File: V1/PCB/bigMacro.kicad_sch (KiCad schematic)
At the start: 24 parts, among them SW1 SW_Push, U1 ATmega32U4-A, Y1 16MHz

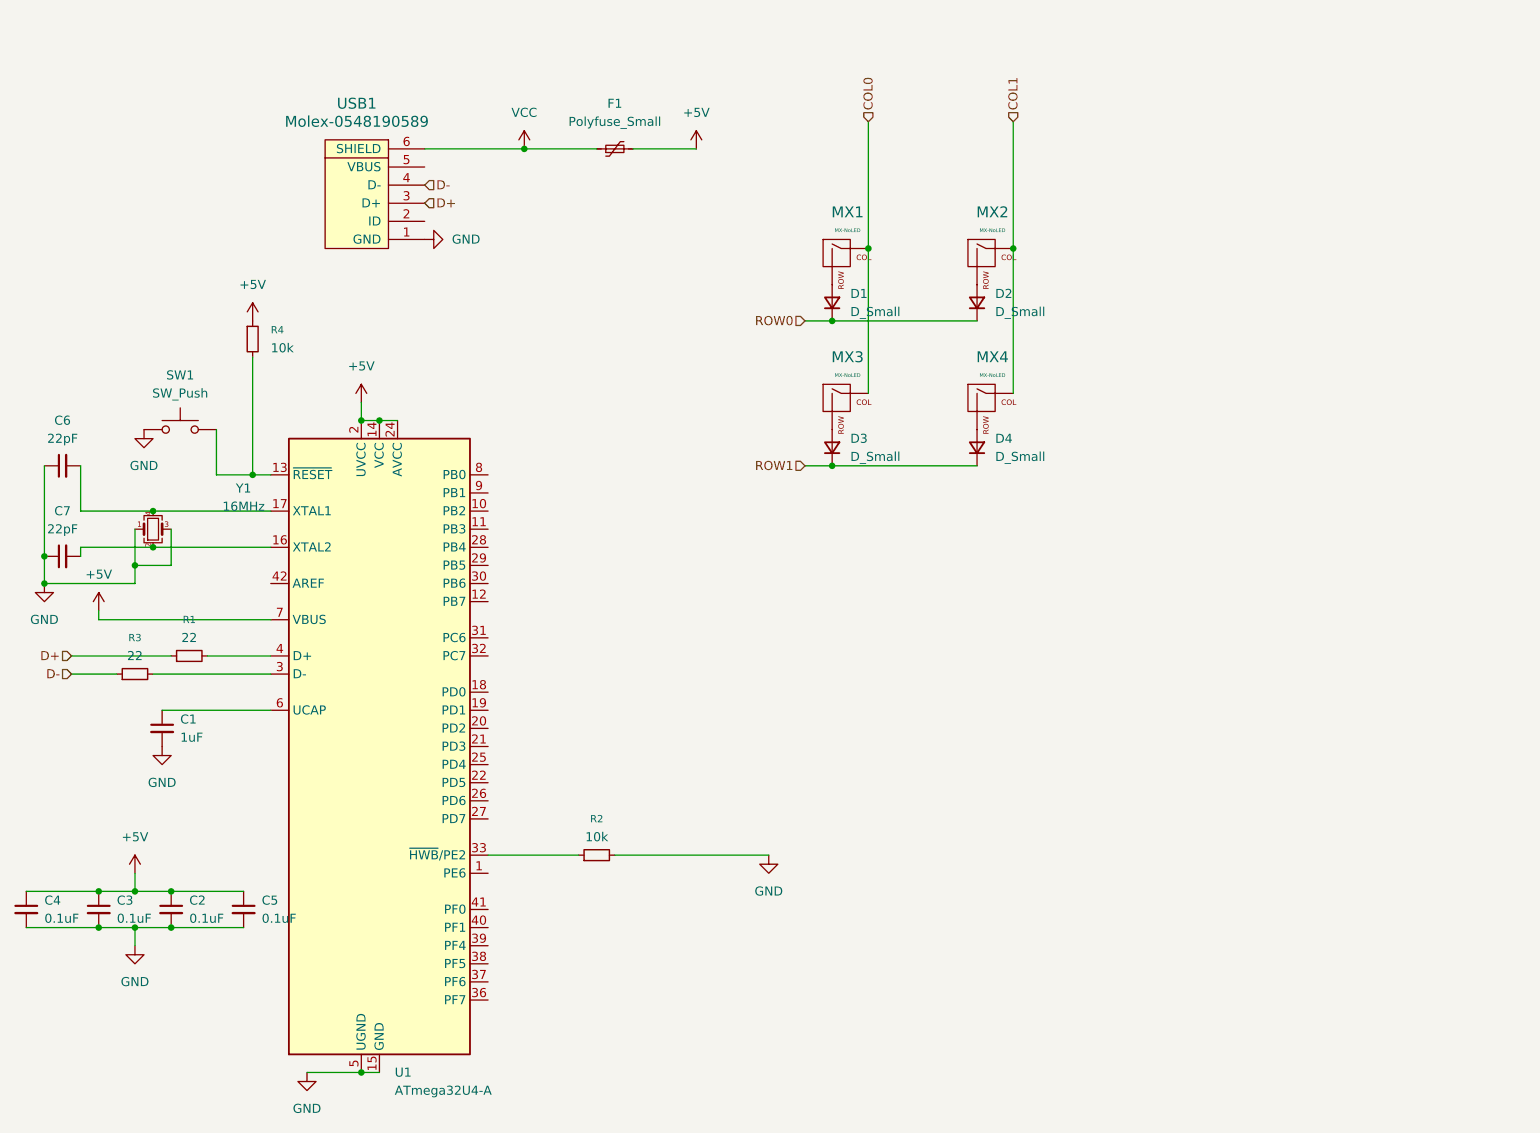
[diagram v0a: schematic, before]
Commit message: Update PCB Layout based on requirements
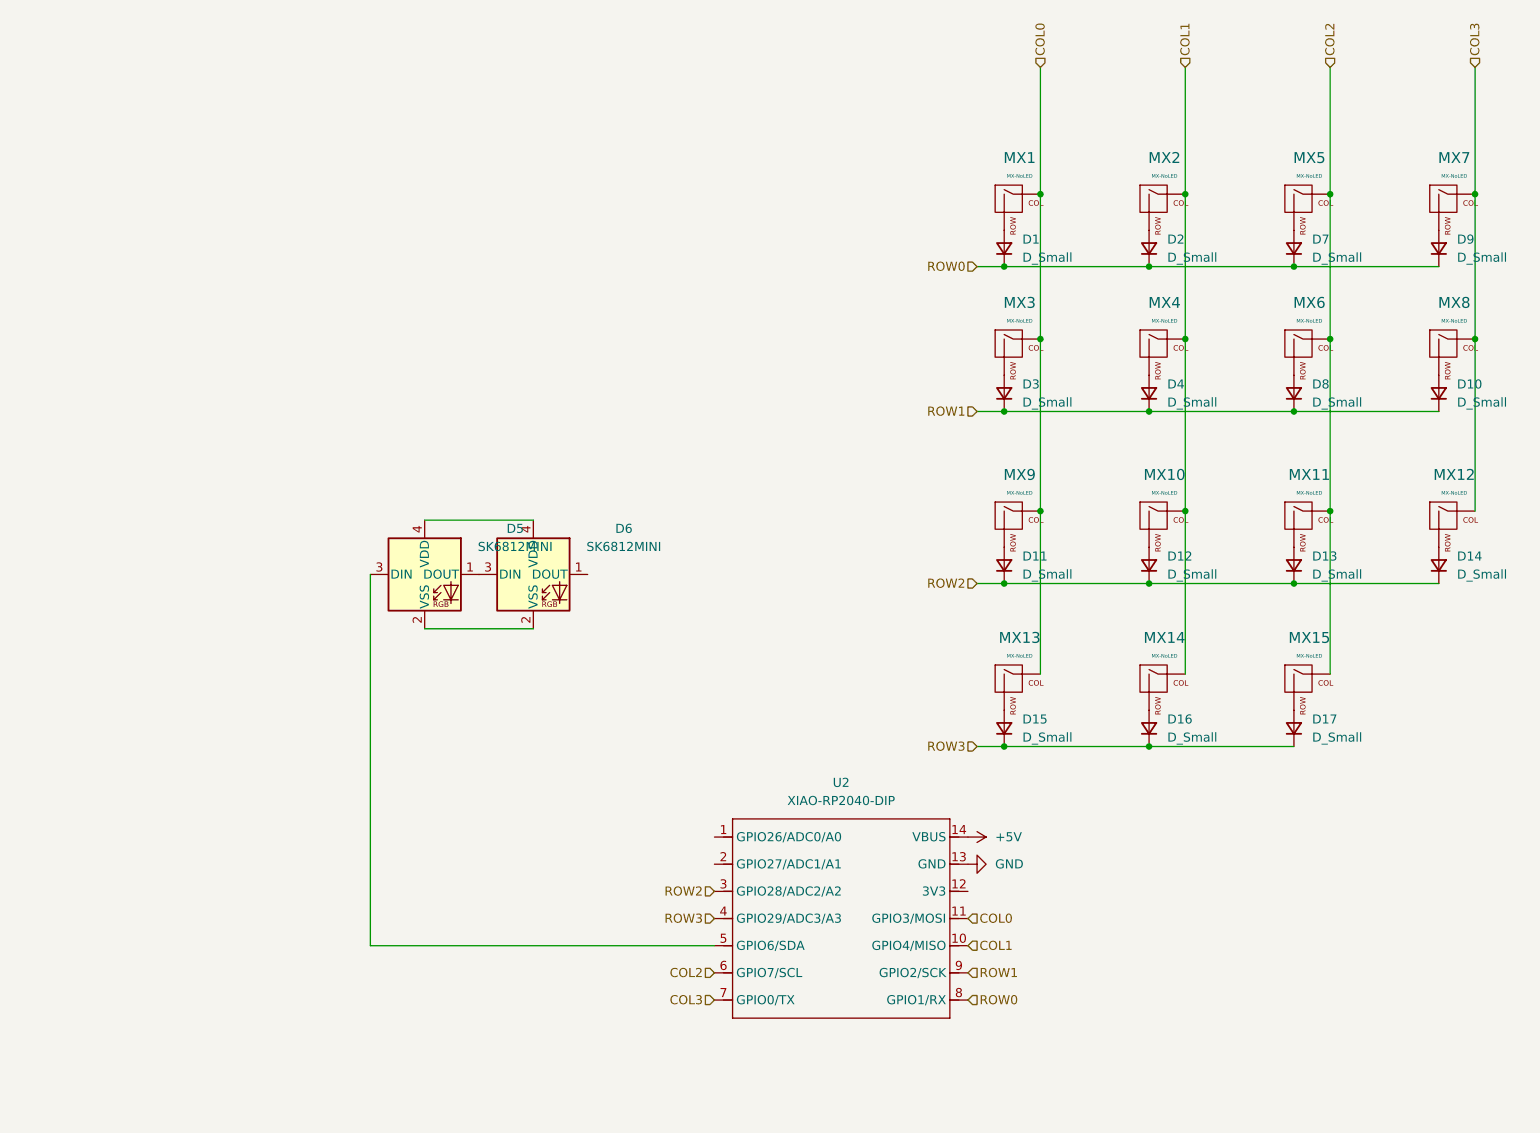
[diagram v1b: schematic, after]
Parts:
- removed C1: 1uF, Capacitor_SMD:C_0805_2012Metric, symbol Device:C_Small
- removed C2, C3, C4, C5: 0.1uF, Capacitor_SMD:C_0805_2012Metric, symbol Device:C_Small
- removed C6, C7: 22pF, Capacitor_SMD:C_0805_2012Metric, symbol Device:C_Small
- removed F1: Polyfuse_Small, Fuse:Fuse_1206_3216Metric, symbol Device:Polyfuse_Small
- removed R1, R3: 22, Resistor_SMD:R_0805_2012Metric, symbol Device:R_Small
- removed R2, R4: 10k, Resistor_SMD:R_0805_2012Metric, symbol Device:R_Small
- removed SW1: SW_Push, Button_Switch_Keyboard:SW_Cherry_MX_1.00u_PCB, symbol Switch:SW_Push
- removed U1: ATmega32U4-A, Package_QFP:TQFP-44_10x10mm_P0.8mm, symbol MCU_Microchip_ATmega:ATmega32U4-A
- removed USB1: Molex-0548190589, PRAND:Molex-0548190589, symbol PRAND:Molex-0548190589
- removed Y1: 16MHz, Crystal:Crystal_SMD_3225-4Pin_3.2x2.5mm, symbol Device:Crystal_GND24_Small
- added D10, D11, D12, D13, D14, D15, D16, D17, D7, D8, D9: D_Small, Diode_SMD:D_SOD-123, symbol Device:D_Small
- added D5, D6: SK6812MINI, LED_SMD:LED_SK6812MINI_PLCC4_3.5x3.5mm_P1.75mm, symbol LED:SK6812MINI
- added MX10, MX11, MX12, MX13, MX14, MX15, MX5, MX6, MX7, MX8, MX9: MX-NoLED, Button_Switch_Keyboard:SW_Cherry_MX_1.00u_PCB, symbol MXAH:MX-NoLED
- added U2: XIAO-RP2040-DIP, OPL:XIAO-RP2040-DIP, symbol Seeed_Studio_XIAO_Series:XIAO-RP2040-DIP
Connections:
- net +5V: now also U2.14 (VBUS)
- net COL0: now also MX13.1 (COL), MX9.1 (COL), U2.11 (GPIO3/MOSI)
- net COL1: now also MX10.1 (COL), MX14.1 (COL), U2.10 (GPIO4/MISO)
- net GND: now also U2.13 (GND)
- net ROW0: now also D7.1 (K), D9.1 (K), U2.8 (GPIO1/RX)
- net ROW1: now also D10.1 (K), D8.1 (K), U2.9 (GPIO2/SCK)
- new net: D13.2 (A), MX11.2 (ROW)
- new net: D12.2 (A), MX10.2 (ROW)
- new net: D15.2 (A), MX13.2 (ROW)
- new net: D9.2 (A), MX7.2 (ROW)
- new net: D10.2 (A), MX8.2 (ROW)
- new net: D16.2 (A), MX14.2 (ROW)
- new net: D14.2 (A), MX12.2 (ROW)
- new net: D7.2 (A), MX5.2 (ROW)
- new net: D5.2 (VSS), D6.2 (VSS)
- new net: D5.1 (DOUT), D6.3 (DIN)
- new net: D5.4 (VDD), D6.4 (VDD)
- new net: D8.2 (A), MX6.2 (ROW)
- new net: D5.3 (DIN), U2.5 (GPIO6/SDA)
- new net: D17.2 (A), MX15.2 (ROW)
- new net: D11.2 (A), MX9.2 (ROW)
- new net COL2: MX11.1 (COL), MX15.1 (COL), MX5.1 (COL), MX6.1 (COL), U2.6 (GPIO7/SCL)
- new net COL3: MX12.1 (COL), MX7.1 (COL), MX8.1 (COL), U2.7 (GPIO0/TX)
- new net ROW2: D11.1 (K), D12.1 (K), D13.1 (K), D14.1 (K), U2.3 (GPIO28/ADC2/A2)
- new net ROW3: D15.1 (K), D16.1 (K), D17.1 (K), U2.4 (GPIO29/ADC3/A3)
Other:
- moved on the sheet: D1, D2, D3, D4, MX1, MX2, MX3, MX4
